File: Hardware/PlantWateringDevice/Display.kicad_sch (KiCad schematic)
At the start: 24 parts, among them SW2 SW_Push, U1 MCP6002-xSN, U2 74LVC1G3157, U6 74HC74, U7 74HC4017D

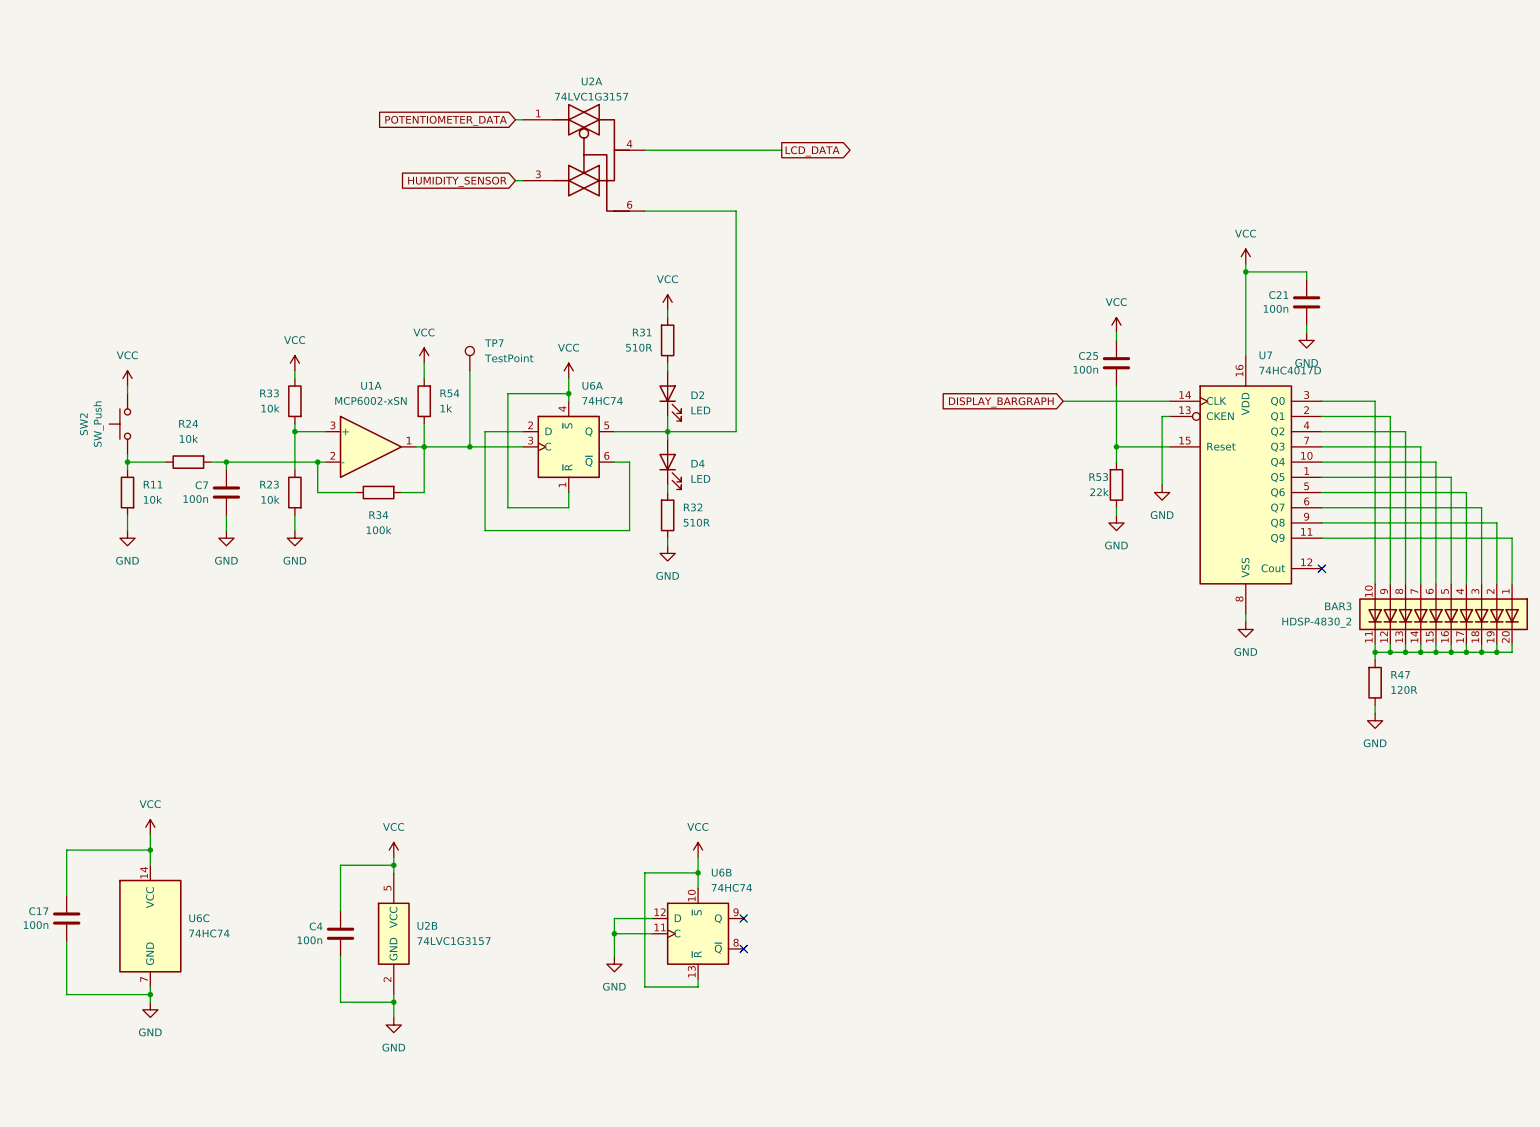
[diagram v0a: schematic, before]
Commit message: fix #16, fix #17, fix #18, fix #19, fix #20, fix #26, fix #27, fix #28, fix #30, fix #32, fix#33, fix #34, fix #35, fix #38
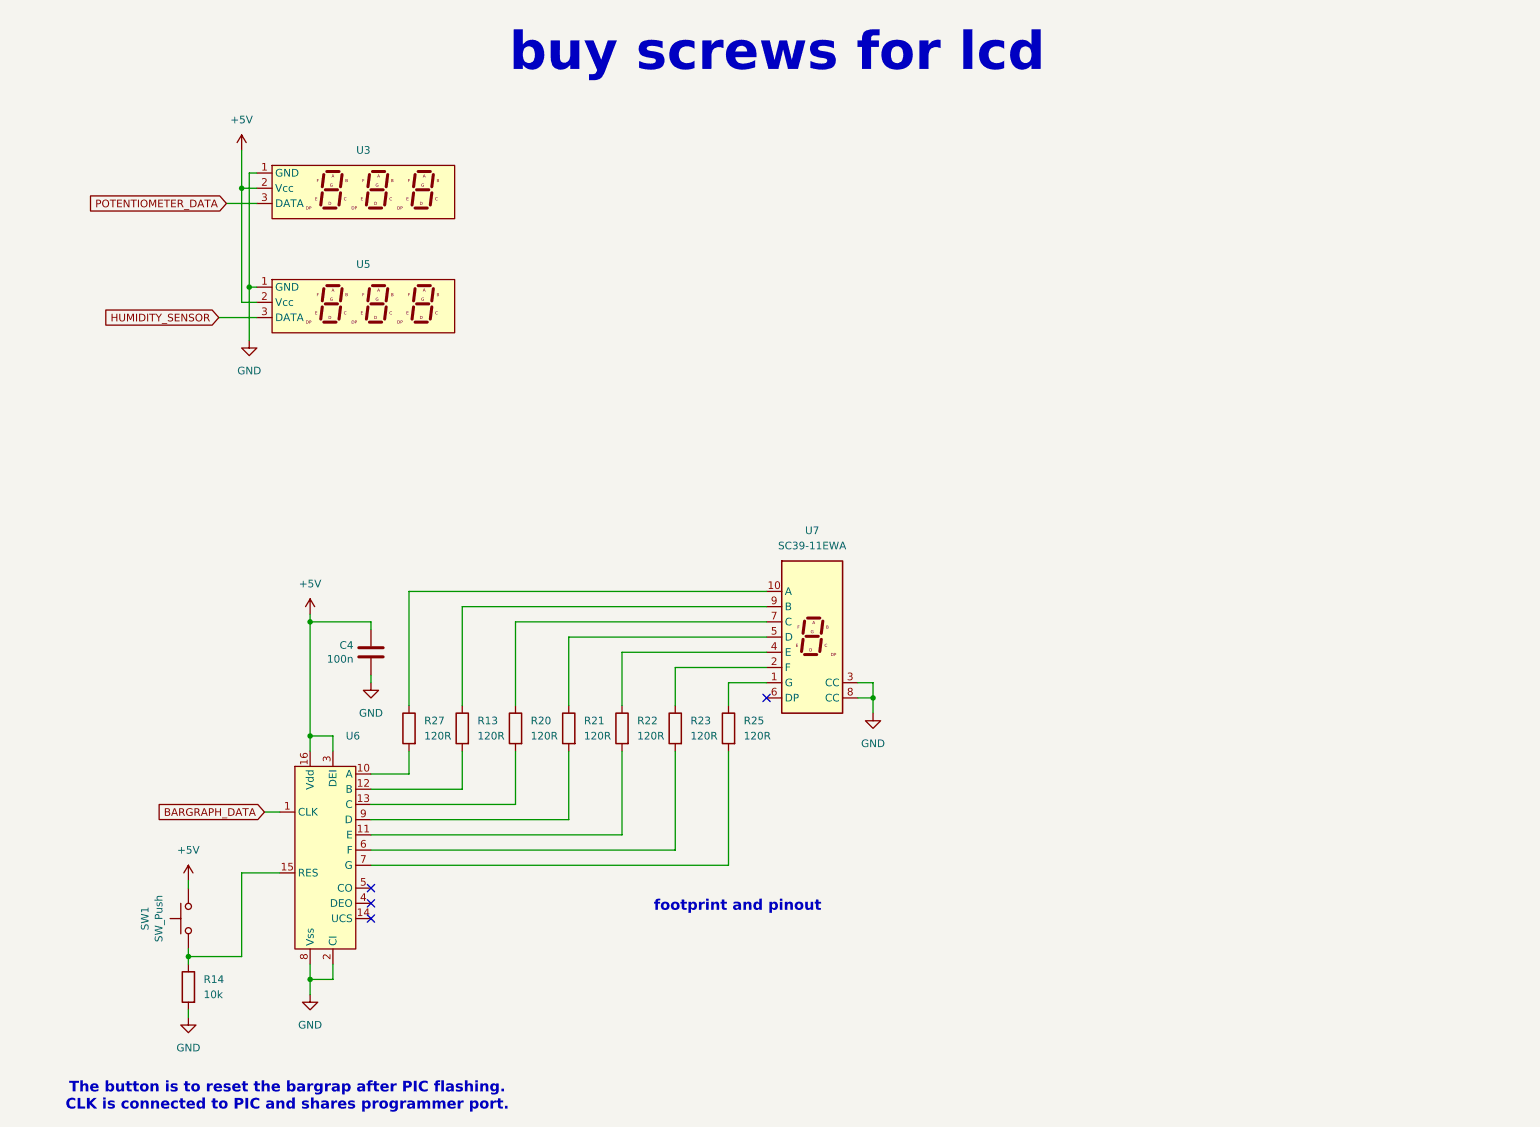
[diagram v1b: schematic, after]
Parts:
- removed BAR3: HDSP-4830_2, Display:HDSP-4830, symbol LED:HDSP-4830_2
- removed C17, C21, C25, C7: 100n, Capacitor_SMD:C_0805_2012Metric, symbol Device:C
- removed D2, D4: LED, LED_THT:LED_D4.0mm, symbol Device:LED
- removed R11, R24, R33: 10k, Resistor_SMD:R_0805_2012Metric, symbol Device:R
- removed R31, R32: 510R, Resistor_SMD:R_0805_2012Metric, symbol Device:R
- removed R34: 100k, Resistor_SMD:R_0805_2012Metric, symbol Device:R
- removed R47: 120R, Resistor_SMD:R_0805_2012Metric, symbol Device:R
- removed R53: 22k, Resistor_SMD:R_0805_2012Metric, symbol Device:R
- removed R54: 1k, Resistor_SMD:R_0805_2012Metric, symbol Device:R
- removed SW2: SW_Push, Button_Switch_SMD:SW_SPST_PTS645Sx43SMTR92, symbol Switch:SW_Push
- removed TP7: TestPoint, TestPoint:TestPoint_Pad_D1.5mm, symbol Connector:TestPoint
- removed U1: MCP6002-xSN, Package_SO:SO-8_3.9x4.9mm_P1.27mm, symbol Amplifier_Operational:MCP6002-xSN
- removed U2: 74LVC1G3157, Package_TO_SOT_SMD:SOT-363_SC-70-6, symbol 74xGxx:74LVC1G3157
- removed U6: 74HC74, Package_SO:SO-14_3.9x8.65mm_P1.27mm, symbol 74xx:74HC74
- removed U7: 74HC4017D, Package_SO:SO-16_3.9x9.9mm_P1.27mm, symbol 4xxx:4017
- added R13, R20, R21, R22, R25, R27: 120R, Resistor_SMD:R_0603_1608Metric, symbol Device:R
- added R14: 10k, Resistor_SMD:R_0603_1608Metric, symbol Device:R
- added SW1: SW_Push, Button_Switch_SMD:SW_SPST_PTS645Sx43SMTR92, symbol Switch:SW_Push
- added U3, U5: (no value), PlantWateringDevice:SegmentDisplayMounting, symbol PlantWateringDevice:LCD_DISPLAY
- added U6: (no value), Package_SO:JEITA_SOIC-16_3.9x9.9mm_P1.27mm, symbol PlantWateringDevice:CD4026
- added U7: SC39-11EWA, Display_7Segment:Sx39-1xxxxx, symbol Display_Character:SC39-11EWA
- C4: footprint Capacitor_SMD:C_0805_2012Metric -> Capacitor_SMD:C_0603_1608Metric
- R23: value 10k -> 120R; footprint Resistor_SMD:R_0805_2012Metric -> Resistor_SMD:R_0603_1608Metric
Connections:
- net GND: now also R14.2, U3.1 (GND), U5.1 (GND), U6.2 (CI), U6.8 (Vss), U7.3 (CC), U7.8 (CC); no longer R23.2
- net HUMIDITY_SENSOR: now also U5.3 (DATA)
- net POTENTIOMETER_DATA: now also U3.3 (DATA)
- net at R23.1: now also U7.2 (F)
- net VCC renamed +5V
- net +5V: now also SW1.2, U3.2 (Vcc), U5.2 (Vcc), U6.16 (Vdd), U6.3 (DEI)
- new net: R13.1, U7.9 (B)
- new net: R13.2, U6.12 (B)
- new net: R25.1, U7.1 (G)
- new net: R27.1, U7.10 (A)
- new net: R22.1, U7.4 (E)
- new net: R21.1, U7.5 (D)
- new net: R20.1, U7.7 (C)
- new net: R27.2, U6.10 (A)
- new net: R22.2, U6.11 (E)
- new net: R20.2, U6.13 (C)
- new net: R14.1, SW1.1, U6.15 (RES)
- new net: R23.2, U6.6 (F)
- new net: R25.2, U6.7 (G)
- new net: R21.2, U6.9 (D)
- new net BARGRAPH_DATA: U6.1 (CLK)
- no-connect marks 3 -> 4
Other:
- note added: "The button is to reset the bargrap after PIC flashing. CLK is connected to PIC and shares programmer port."
- note added: "buy screws for lcd"
- note added: "footprint and pinout"
